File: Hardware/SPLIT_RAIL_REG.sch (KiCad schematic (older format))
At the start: 21 parts, among them Q1 PMOS, U1 TPS65130

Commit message: Annotated schematic
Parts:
- renumbered C2 to C1, C8 to C2, C9 to C3, C7 to C4, C6 to C5, C1 to C6, C3 to C7, C4 to C8, C5 to C9, R4 to R1, R5 to R3, R3 to R4, R1 to R5
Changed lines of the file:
@@
 LIBS:microchip_pic18mcu
 LIBS:microchip
+LIBS:microchip1
 LIBS:microcontrollers
 LIBS:motorola
@@
 LIBS:sensors
 LIBS:siliconi
+LIBS:special
 LIBS:stm8
 LIBS:stm32
@@
 $EndComp
 $Comp
-L GND-RESCUE-museV2 #PWR5
+L GND-RESCUE-museV2-RESCUE-museV2 #PWR01
 U 1 1 57DAC9F2
 P 5450 5000
-F 0 "#PWR5" H 5450 4750 50  0001 C CNN
+F 0 "#PWR01" H 5450 4750 50  0001 C CNN
 F 1 "GND" H 5450 4850 50  0000 C CNN
 F 2 "" H 5450 5000 50  0000 C CNN
@@
 $EndComp
 $Comp
-L C-RESCUE-museV2 C4
+L C-RESCUE-museV2 C8
 U 1 1 57DACA1F
 P 6100 4750
-F 0 "C4" H 6125 4850 50  0000 L CNN
+F 0 "C8" H 6125 4850 50  0000 L CNN
 F 1 "10nF" H 6125 4650 50  0000 L CNN
 F 2 "" H 6138 4600 50  0000 C CNN
@@
 $EndComp
 $Comp
-L C-RESCUE-museV2 C5
+L C-RESCUE-museV2 C9
 U 1 1 57DACA4A
 P 6350 4750
-F 0 "C5" H 6375 4850 50  0000 L CNN
+F 0 "C9" H 6375 4850 50  0000 L CNN
 F 1 "4.7nF" H 6375 4650 50  0000 L CNN
 F 2 "" H 6388 4600 50  0000 C CNN
@@
 $EndComp
 $Comp
-L GND-RESCUE-museV2 #PWR6
+L GND-RESCUE-museV2-RESCUE-museV2 #PWR02
 U 1 1 57DACA83
 P 6100 5000
-F 0 "#PWR6" H 6100 4750 50  0001 C CNN
+F 0 "#PWR02" H 6100 4750 50  0001 C CNN
 F 1 "GND" H 6100 4850 50  0000 C CNN
 F 2 "" H 6100 5000 50  0000 C CNN
@@
 $EndComp
 $Comp
-L GND-RESCUE-museV2 #PWR7
+L GND-RESCUE-museV2-RESCUE-museV2 #PWR03
 U 1 1 57DACA97
 P 6350 5000
-F 0 "#PWR7" H 6350 4750 50  0001 C CNN
+F 0 "#PWR03" H 6350 4750 50  0001 C CNN
 F 1 "GND" H 6350 4850 50  0000 C CNN
 F 2 "" H 6350 5000 50  0000 C CNN
@@
 $EndComp
 $Comp
-L GND-RESCUE-museV2 #PWR8
+L GND-RESCUE-museV2-RESCUE-museV2 #PWR04
 U 1 1 57DACC08
 P 6600 5000
-F 0 "#PWR8" H 6600 4750 50  0001 C CNN
+F 0 "#PWR04" H 6600 4750 50  0001 C CNN
 F 1 "GND" H 6600 4850 50  0000 C CNN
 F 2 "" H 6600 5000 50  0000 C CNN
@@
 $EndComp
 $Comp
-L GND-RESCUE-museV2 #PWR12
+L GND-RESCUE-museV2-RESCUE-museV2 #PWR05
 U 1 1 57DACD4E
 P 7550 5000
-F 0 "#PWR12" H 7550 4750 50  0001 C CNN
+F 0 "#PWR05" H 7550 4750 50  0001 C CNN
 F 1 "GND" H 7550 4850 50  0000 C CNN
 F 2 "" H 7550 5000 50  0000 C CNN
@@
 Connection ~ 6100 4200
 $Comp
-L R-RESCUE-museV2 R3
+L R-RESCUE-museV2 R4
 U 1 1 57DACF39
 P 6300 3800
-F 0 "R3" V 6200 3800 50  0000 C CNN
+F 0 "R4" V 6200 3800 50  0000 C CNN
 F 1 "1.3M" V 6300 3800 50  0000 C CNN
 F 2 "" V 6230 3800 50  0000 C CNN
@@
 $EndComp
 $Comp
-L C-RESCUE-museV2 C6
+L C-RESCUE-museV2 C5
 U 1 1 57DACF8B
 P 6500 3800
-F 0 "C6" H 6525 3900 50  0000 L CNN
+F 0 "C5" H 6525 3900 50  0000 L CNN
 F 1 "7.5pF" H 6525 3700 50  0000 L CNN
 F 2 "" H 6538 3650 50  0000 C CNN
@@
 	6300 3200 6300 3250
 $Comp
-L C-RESCUE-museV2 C7
+L C-RESCUE-museV2 C4
 U 1 1 57DADA01
 P 6850 3400
-F 0 "C7" H 6875 3500 50  0000 L CNN
+F 0 "C4" H 6875 3500 50  0000 L CNN
 F 1 "220nF" H 6875 3300 50  0000 L CNN
 F 2 "" H 6888 3250 50  0000 C CNN
@@
 Connection ~ 6300 3200
 $Comp
-L GND-RESCUE-museV2 #PWR9
+L GND-RESCUE-museV2-RESCUE-museV2 #PWR06
 U 1 1 57DADA89
 P 6850 3750
-F 0 "#PWR9" H 6850 3500 50  0001 C CNN
+F 0 "#PWR06" H 6850 3500 50  0001 C CNN
 F 1 "GND" H 6850 3600 50  0000 C CNN
 F 2 "" H 6850 3750 50  0000 C CNN
@@
 Connection ~ 4800 4200
 $Comp
-L C-RESCUE-museV2 C3
+L C-RESCUE-museV2 C7
 U 1 1 57DAE032
 P 4550 4750
-F 0 "C3" H 4575 4850 50  0000 L CNN
+F 0 "C7" H 4575 4850 50  0000 L CNN
 F 1 "100nF" H 4575 4650 50  0000 L CNN
 F 2 "" H 4588 4600 50  0000 C CNN
@@
 Connection ~ 4800 4500
 $Comp
-L R-RESCUE-museV2 R1
+L R-RESCUE-museV2 R5
 U 1 1 57DAE140
 P 4300 4500
-F 0 "R1" V 4380 4500 50  0000 C CNN
+F 0 "R5" V 4380 4500 50  0000 C CNN
 F 1 "100" V 4300 4500 50  0000 C CNN
 F 2 "" V 4230 4500 50  0000 C CNN
@@
 	4050 4500 4150 4500
 $Comp
-L GND-RESCUE-museV2 #PWR4
+L GND-RESCUE-museV2-RESCUE-museV2 #PWR07
 U 1 1 57DAE30A
 P 4550 5000
-F 0 "#PWR4" H 4550 4750 50  0001 C CNN
+F 0 "#PWR07" H 4550 4750 50  0001 C CNN
 F 1 "GND" H 4550 4850 50  0000 C CNN
 F 2 "" H 4550 5000 50  0000 C CNN
@@
 	4550 5000 4550 4900
 $Comp
-L GND-RESCUE-museV2 #PWR2
+L GND-RESCUE-museV2-RESCUE-museV2 #PWR08
 U 1 1 57DAE3B0
 P 4050 5000
-F 0 "#PWR2" H 4050 4750 50  0001 C CNN
+F 0 "#PWR08" H 4050 4750 50  0001 C CNN
 F 1 "GND" H 4050 4850 50  0000 C CNN
 F 2 "" H 4050 5000 50  0000 C CNN
@@
 Connection ~ 4550 2550
 $Comp
-L C-RESCUE-museV2 C2
+L C-RESCUE-museV2 C1
 U 1 1 57DAEAFC
 P 4550 2850
-F 0 "C2" H 4575 2950 50  0000 L CNN
+F 0 "C1" H 4575 2950 50  0000 L CNN
 F 1 "4.7uF" H 4575 2750 50  0000 L CNN
 F 2 "" H 4588 2700 50  0000 C CNN
@@
 $EndComp
 $Comp
-L GND-RESCUE-museV2 #PWR3
+L GND-RESCUE-museV2-RESCUE-museV2 #PWR09
 U 1 1 57DAEBCD
 P 4550 3050
-F 0 "#PWR3" H 4550 2800 50  0001 C CNN
+F 0 "#PWR09" H 4550 2800 50  0001 C CNN
 F 1 "GND" H 4550 2900 50  0000 C CNN
 F 2 "" H 4550 3050 50  0000 C CNN
@@
 Connection ~ 6100 2550
 $Comp
-L R-RESCUE-museV2 R5
+L R-RESCUE-museV2 R3
 U 1 1 57DAF2BE
 P 7250 3400
-F 0 "R5" V 7330 3400 50  0000 C CNN
+F 0 "R3" V 7330 3400 50  0000 C CNN
 F 1 "85.8k" V 7150 3400 50  0000 C CNN
 F 2 "" V 7180 3400 50  0000 C CNN
@@
 $EndComp
 $Comp
-L GND-RESCUE-museV2 #PWR10
+L GND-RESCUE-museV2-RESCUE-museV2 #PWR010
 U 1 1 57DAF32E
 P 7250 3750
-F 0 "#PWR10" H 7250 3500 50  0001 C CNN
+F 0 "#PWR010" H 7250 3500 50  0001 C CNN
 F 1 "GND" H 7250 3600 50  0000 C CNN
 F 2 "" H 7250 3750 50  0000 C CNN
@@
 	7250 3000 7250 3250
 $Comp
-L R-RESCUE-museV2 R4
+L R-RESCUE-museV2 R1
 U 1 1 57DAF532
 P 7050 2850
-F 0 "R4" V 7130 2850 50  0000 C CNN
+F 0 "R1" V 7130 2850 50  0000 C CNN
 F 1 "975k" V 7050 2850 50  0000 C CNN
 F 2 "" V 6980 2850 50  0000 C CNN
@@
 Connection ~ 7250 2550
 $Comp
-L C-RESCUE-museV2 C8
+L C-RESCUE-museV2 C2
 U 1 1 57DAF6D3
 P 7250 2850
-F 0 "C8" H 7275 2950 50  0000 L CNN
+F 0 "C2" H 7275 2950 50  0000 L CNN
 F 1 "6.8pF" H 7275 2750 50  0000 L CNN
 F 2 "" H 7288 2700 50  0000 C CNN
@@
 $EndComp
 $Comp
-L C-RESCUE-museV2 C9
+L C-RESCUE-museV2 C3
 U 1 1 57DAF88B
 P 7550 2850
-F 0 "C9" H 7575 2950 50  0000 L CNN
+F 0 "C3" H 7575 2950 50  0000 L CNN
 F 1 "4.7uF" H 7575 2750 50  0000 L CNN
 F 2 "" H 7588 2700 50  0000 C CNN
@@
 Connection ~ 7550 2550
 $Comp
-L GND-RESCUE-museV2 #PWR11
+L GND-RESCUE-museV2-RESCUE-museV2 #PWR011
 U 1 1 57DAF96B
 P 7550 3750
-F 0 "#PWR11" H 7550 3500 50  0001 C CNN
+F 0 "#PWR011" H 7550 3500 50  0001 C CNN
 F 1 "GND" H 7550 3600 50  0000 C CNN
 F 2 "" H 7550 3750 50  0000 C CNN
@@
 	7550 3750 7550 3000
 $Comp
-L C-RESCUE-museV2 C1
+L C-RESCUE-museV2 C6
 U 1 1 57DB07FA
 P 4050 4750
-F 0 "C1" H 4075 4850 50  0000 L CNN
+F 0 "C6" H 4075 4850 50  0000 L CNN
 F 1 "4.7uF" H 4075 4650 50  0000 L CNN
 F 2 "" H 4088 4600 50  0000 C CNN
@@
 UNSURE OF C75, C77 VALUES
 $Comp
-L +5VSB #PWR1
+L +5VSB #PWR012
 U 1 1 57F87DFC
 P 4050 2300
-F 0 "#PWR1" H 4050 2390 20  0001 C CNN
+F 0 "#PWR012" H 4050 2390 20  0001 C CNN
 F 1 "+5VSB" H 4050 2390 30  0000 C CNN
 F 2 "" H 4050 2300 60  0000 C CNN
@@
 	5550 2550 7850 2550
 $Comp
-L -15VSB #PWR14
+L -15VSB #PWR7
 U 1 1 57F88303
 P 7850 4200
-F 0 "#PWR14" H 7850 4300 50  0001 C CNN
+F 0 "#PWR7" H 7850 4300 50  0001 C CNN
 F 1 "-15VSB" H 7850 4350 50  0000 C CNN
 F 2 "" H 7850 4200 50  0000 C CNN
@@
 	7850 2550 7850 2300
 $Comp
-L +15VSB #PWR13
+L +15VSB #PWR013
 U 1 1 57F88166
 P 7850 2300
-F 0 "#PWR13" H 7850 2150 50  0001 C CNN
+F 0 "#PWR013" H 7850 2150 50  0001 C CNN
 F 1 "+15VSB" H 7850 2440 50  0000 C CNN
 F 2 "" H 7850 2300 50  0000 C CNN

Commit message: Annotation/Part Selection BOM Update
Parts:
- C2: value 6.8pF -> 6.97pF
- C5: value 7.5pF -> 5.77pF
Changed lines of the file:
@@
 LIBS:microchip_pic18mcu
 LIBS:microchip
+LIBS:microchip1
 LIBS:microcontrollers
 LIBS:motorola
@@
 LIBS:sensors
 LIBS:siliconi
+LIBS:special
 LIBS:stm8
 LIBS:stm32
@@
 $EndComp
 $Comp
-L GND-RESCUE-museV2-RESCUE-museV2 #PWR5
+L GND-RESCUE-museV2-RESCUE-museV2 #PWR01
 U 1 1 57DAC9F2
 P 5450 5000
-F 0 "#PWR5" H 5450 4750 50  0001 C CNN
+F 0 "#PWR01" H 5450 4750 50  0001 C CNN
 F 1 "GND" H 5450 4850 50  0000 C CNN
 F 2 "" H 5450 5000 50  0000 C CNN
@@
 $EndComp
 $Comp
-L GND-RESCUE-museV2-RESCUE-museV2 #PWR6
+L GND-RESCUE-museV2-RESCUE-museV2 #PWR02
 U 1 1 57DACA83
 P 6100 5000
-F 0 "#PWR6" H 6100 4750 50  0001 C CNN
+F 0 "#PWR02" H 6100 4750 50  0001 C CNN
 F 1 "GND" H 6100 4850 50  0000 C CNN
 F 2 "" H 6100 5000 50  0000 C CNN
@@
 $EndComp
 $Comp
-L GND-RESCUE-museV2-RESCUE-museV2 #PWR7
+L GND-RESCUE-museV2-RESCUE-museV2 #PWR03
 U 1 1 57DACA97
 P 6350 5000
-F 0 "#PWR7" H 6350 4750 50  0001 C CNN
+F 0 "#PWR03" H 6350 4750 50  0001 C CNN
 F 1 "GND" H 6350 4850 50  0000 C CNN
 F 2 "" H 6350 5000 50  0000 C CNN
@@
 $EndComp
 $Comp
-L GND-RESCUE-museV2-RESCUE-museV2 #PWR8
+L GND-RESCUE-museV2-RESCUE-museV2 #PWR04
 U 1 1 57DACC08
 P 6600 5000
-F 0 "#PWR8" H 6600 4750 50  0001 C CNN
+F 0 "#PWR04" H 6600 4750 50  0001 C CNN
 F 1 "GND" H 6600 4850 50  0000 C CNN
 F 2 "" H 6600 5000 50  0000 C CNN
@@
 $EndComp
 $Comp
-L GND-RESCUE-museV2-RESCUE-museV2 #PWR12
+L GND-RESCUE-museV2-RESCUE-museV2 #PWR05
 U 1 1 57DACD4E
 P 7550 5000
-F 0 "#PWR12" H 7550 4750 50  0001 C CNN
+F 0 "#PWR05" H 7550 4750 50  0001 C CNN
 F 1 "GND" H 7550 4850 50  0000 C CNN
 F 2 "" H 7550 5000 50  0000 C CNN
@@
 P 6500 3800
 F 0 "C5" H 6525 3900 50  0000 L CNN
-F 1 "7.5pF" H 6525 3700 50  0000 L CNN
+F 1 "5.77pF" H 6525 3700 50  0000 L CNN
 F 2 "" H 6538 3650 50  0000 C CNN
 F 3 "" H 6500 3800 50  0000 C CNN
@@
 Connection ~ 6300 3200
 $Comp
-L GND-RESCUE-museV2-RESCUE-museV2 #PWR9
+L GND-RESCUE-museV2-RESCUE-museV2 #PWR06
 U 1 1 57DADA89
 P 6850 3750
-F 0 "#PWR9" H 6850 3500 50  0001 C CNN
+F 0 "#PWR06" H 6850 3500 50  0001 C CNN
 F 1 "GND" H 6850 3600 50  0000 C CNN
 F 2 "" H 6850 3750 50  0000 C CNN
@@
 	4050 4500 4150 4500
 $Comp
-L GND-RESCUE-museV2-RESCUE-museV2 #PWR4
+L GND-RESCUE-museV2-RESCUE-museV2 #PWR07
 U 1 1 57DAE30A
 P 4550 5000
-F 0 "#PWR4" H 4550 4750 50  0001 C CNN
+F 0 "#PWR07" H 4550 4750 50  0001 C CNN
 F 1 "GND" H 4550 4850 50  0000 C CNN
 F 2 "" H 4550 5000 50  0000 C CNN
@@
 	4550 5000 4550 4900
 $Comp
-L GND-RESCUE-museV2-RESCUE-museV2 #PWR2
+L GND-RESCUE-museV2-RESCUE-museV2 #PWR08
 U 1 1 57DAE3B0
 P 4050 5000
-F 0 "#PWR2" H 4050 4750 50  0001 C CNN
+F 0 "#PWR08" H 4050 4750 50  0001 C CNN
 F 1 "GND" H 4050 4850 50  0000 C CNN
 F 2 "" H 4050 5000 50  0000 C CNN
@@
 $EndComp
 $Comp
-L GND-RESCUE-museV2-RESCUE-museV2 #PWR3
+L GND-RESCUE-museV2-RESCUE-museV2 #PWR09
 U 1 1 57DAEBCD
 P 4550 3050
-F 0 "#PWR3" H 4550 2800 50  0001 C CNN
+F 0 "#PWR09" H 4550 2800 50  0001 C CNN
 F 1 "GND" H 4550 2900 50  0000 C CNN
 F 2 "" H 4550 3050 50  0000 C CNN
@@
 $EndComp
 $Comp
-L GND-RESCUE-museV2-RESCUE-museV2 #PWR10
+L GND-RESCUE-museV2-RESCUE-museV2 #PWR010
 U 1 1 57DAF32E
 P 7250 3750
-F 0 "#PWR10" H 7250 3500 50  0001 C CNN
+F 0 "#PWR010" H 7250 3500 50  0001 C CNN
 F 1 "GND" H 7250 3600 50  0000 C CNN
 F 2 "" H 7250 3750 50  0000 C CNN
@@
 P 7250 2850
 F 0 "C2" H 7275 2950 50  0000 L CNN
-F 1 "6.8pF" H 7275 2750 50  0000 L CNN
+F 1 "6.97pF" H 7275 2750 50  0000 L CNN
 F 2 "" H 7288 2700 50  0000 C CNN
 F 3 "" H 7250 2850 50  0000 C CNN
@@
 Connection ~ 7550 2550
 $Comp
-L GND-RESCUE-museV2-RESCUE-museV2 #PWR11
+L GND-RESCUE-museV2-RESCUE-museV2 #PWR011
 U 1 1 57DAF96B
 P 7550 3750
-F 0 "#PWR11" H 7550 3500 50  0001 C CNN
+F 0 "#PWR011" H 7550 3500 50  0001 C CNN
 F 1 "GND" H 7550 3600 50  0000 C CNN
 F 2 "" H 7550 3750 50  0000 C CNN
@@
 UNSURE OF C75, C77 VALUES
 $Comp
-L +5VSB #PWR1
+L +5VSB #PWR012
 U 1 1 57F87DFC
 P 4050 2300
-F 0 "#PWR1" H 4050 2390 20  0001 C CNN
+F 0 "#PWR012" H 4050 2390 20  0001 C CNN
 F 1 "+5VSB" H 4050 2390 30  0000 C CNN
 F 2 "" H 4050 2300 60  0000 C CNN
@@
 	7850 2550 7850 2300
 $Comp
-L +15VSB #PWR13
+L +15VSB #PWR013
 U 1 1 57F88166
 P 7850 2300
-F 0 "#PWR13" H 7850 2150 50  0001 C CNN
+F 0 "#PWR013" H 7850 2150 50  0001 C CNN
 F 1 "+15VSB" H 7850 2440 50  0000 C CNN
 F 2 "" H 7850 2300 50  0000 C CNN

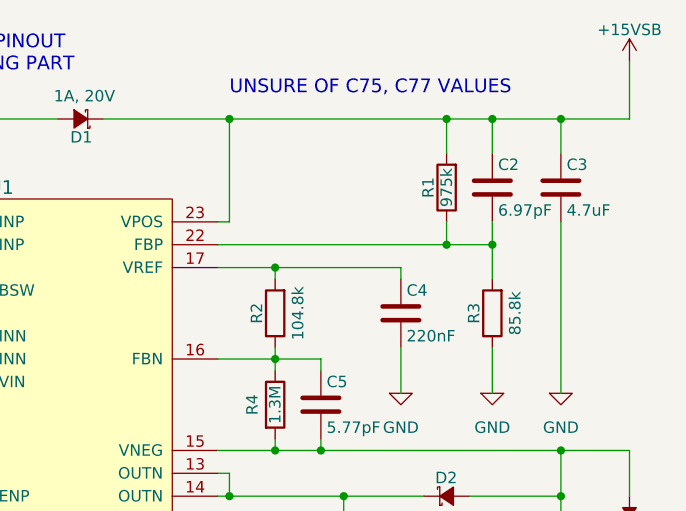
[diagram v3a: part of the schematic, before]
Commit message: Added bluetooth pair button
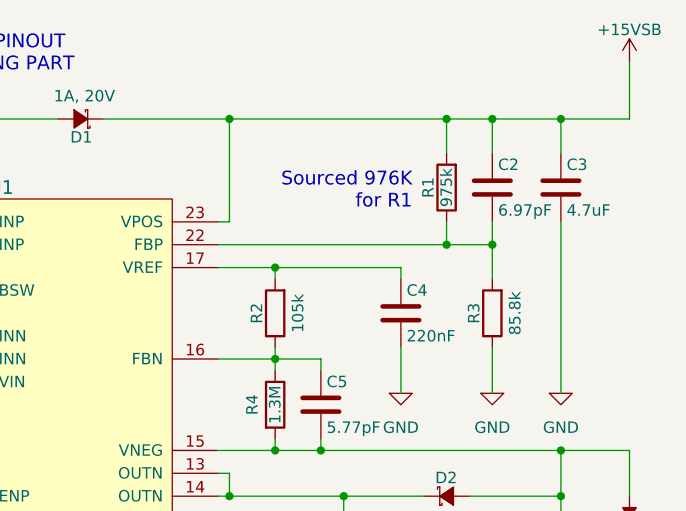
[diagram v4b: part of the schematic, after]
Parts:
- R2: value 104.8k -> 105k
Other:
- note added: "Sourced 976K\nfor R1"
- note removed: "UNSURE OF C75, C77 VALUES"
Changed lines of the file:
@@
 $EndComp
 $Comp
-L GND-RESCUE-museV2-RESCUE-museV2 #PWR01
+L GND-RESCUE-museV2-RESCUE-museV2 #PWR10
 U 1 1 57DAC9F2
 P 5450 5000
-F 0 "#PWR01" H 5450 4750 50  0001 C CNN
+F 0 "#PWR10" H 5450 4750 50  0001 C CNN
 F 1 "GND" H 5450 4850 50  0000 C CNN
 F 2 "" H 5450 5000 50  0000 C CNN
@@
 $EndComp
 $Comp
-L GND-RESCUE-museV2-RESCUE-museV2 #PWR02
+L GND-RESCUE-museV2-RESCUE-museV2 #PWR11
 U 1 1 57DACA83
 P 6100 5000
-F 0 "#PWR02" H 6100 4750 50  0001 C CNN
+F 0 "#PWR11" H 6100 4750 50  0001 C CNN
 F 1 "GND" H 6100 4850 50  0000 C CNN
 F 2 "" H 6100 5000 50  0000 C CNN
@@
 $EndComp
 $Comp
-L GND-RESCUE-museV2-RESCUE-museV2 #PWR03
+L GND-RESCUE-museV2-RESCUE-museV2 #PWR12
 U 1 1 57DACA97
 P 6350 5000
-F 0 "#PWR03" H 6350 4750 50  0001 C CNN
+F 0 "#PWR12" H 6350 4750 50  0001 C CNN
 F 1 "GND" H 6350 4850 50  0000 C CNN
 F 2 "" H 6350 5000 50  0000 C CNN
@@
 $EndComp
 $Comp
-L GND-RESCUE-museV2-RESCUE-museV2 #PWR04
+L GND-RESCUE-museV2-RESCUE-museV2 #PWR13
 U 1 1 57DACC08
 P 6600 5000
-F 0 "#PWR04" H 6600 4750 50  0001 C CNN
+F 0 "#PWR13" H 6600 4750 50  0001 C CNN
 F 1 "GND" H 6600 4850 50  0000 C CNN
 F 2 "" H 6600 5000 50  0000 C CNN
@@
 $EndComp
 $Comp
-L GND-RESCUE-museV2-RESCUE-museV2 #PWR05
+L GND-RESCUE-museV2-RESCUE-museV2 #PWR14
 U 1 1 57DACD4E
 P 7550 5000
-F 0 "#PWR05" H 7550 4750 50  0001 C CNN
+F 0 "#PWR14" H 7550 4750 50  0001 C CNN
 F 1 "GND" H 7550 4850 50  0000 C CNN
 F 2 "" H 7550 5000 50  0000 C CNN
@@
 P 6300 3400
 F 0 "R2" V 6380 3400 50  0000 C CNN
-F 1 "104.8k" V 6200 3400 50  0000 C CNN
+F 1 "105k" V 6200 3400 50  0000 C CNN
 F 2 "" V 6230 3400 50  0000 C CNN
 F 3 "" H 6300 3400 50  0000 C CNN
@@
 Connection ~ 6300 3200
 $Comp
-L GND-RESCUE-museV2-RESCUE-museV2 #PWR06
+L GND-RESCUE-museV2-RESCUE-museV2 #PWR4
 U 1 1 57DADA89
 P 6850 3750
-F 0 "#PWR06" H 6850 3500 50  0001 C CNN
+F 0 "#PWR4" H 6850 3500 50  0001 C CNN
 F 1 "GND" H 6850 3600 50  0000 C CNN
 F 2 "" H 6850 3750 50  0000 C CNN
@@
 	4050 4500 4150 4500
 $Comp
-L GND-RESCUE-museV2-RESCUE-museV2 #PWR07
+L GND-RESCUE-museV2-RESCUE-museV2 #PWR9
 U 1 1 57DAE30A
 P 4550 5000
-F 0 "#PWR07" H 4550 4750 50  0001 C CNN
+F 0 "#PWR9" H 4550 4750 50  0001 C CNN
 F 1 "GND" H 4550 4850 50  0000 C CNN
 F 2 "" H 4550 5000 50  0000 C CNN
@@
 	4550 5000 4550 4900
 $Comp
-L GND-RESCUE-museV2-RESCUE-museV2 #PWR08
+L GND-RESCUE-museV2-RESCUE-museV2 #PWR8
 U 1 1 57DAE3B0
 P 4050 5000
-F 0 "#PWR08" H 4050 4750 50  0001 C CNN
+F 0 "#PWR8" H 4050 4750 50  0001 C CNN
 F 1 "GND" H 4050 4850 50  0000 C CNN
 F 2 "" H 4050 5000 50  0000 C CNN
@@
 $EndComp
 $Comp
-L GND-RESCUE-museV2-RESCUE-museV2 #PWR09
+L GND-RESCUE-museV2-RESCUE-museV2 #PWR3
 U 1 1 57DAEBCD
 P 4550 3050
-F 0 "#PWR09" H 4550 2800 50  0001 C CNN
+F 0 "#PWR3" H 4550 2800 50  0001 C CNN
 F 1 "GND" H 4550 2900 50  0000 C CNN
 F 2 "" H 4550 3050 50  0000 C CNN
@@
 $EndComp
 $Comp
-L GND-RESCUE-museV2-RESCUE-museV2 #PWR010
+L GND-RESCUE-museV2-RESCUE-museV2 #PWR5
 U 1 1 57DAF32E
 P 7250 3750
-F 0 "#PWR010" H 7250 3500 50  0001 C CNN
+F 0 "#PWR5" H 7250 3500 50  0001 C CNN
 F 1 "GND" H 7250 3600 50  0000 C CNN
 F 2 "" H 7250 3750 50  0000 C CNN
@@
 Connection ~ 7550 2550
 $Comp
-L GND-RESCUE-museV2-RESCUE-museV2 #PWR011
+L GND-RESCUE-museV2-RESCUE-museV2 #PWR6
 U 1 1 57DAF96B
 P 7550 3750
-F 0 "#PWR011" H 7550 3500 50  0001 C CNN
+F 0 "#PWR6" H 7550 3500 50  0001 C CNN
 F 1 "GND" H 7550 3600 50  0000 C CNN
 F 2 "" H 7550 3750 50  0000 C CNN
@@
 	1    0    0    -1
 $EndComp
-Text Notes 6100 2450 0    60   ~ 0
-UNSURE OF C75, C77 VALUES
-$Comp
-L +5VSB #PWR012
+$Comp
+L +5VSB #PWR1
 U 1 1 57F87DFC
 P 4050 2300
-F 0 "#PWR012" H 4050 2390 20  0001 C CNN
+F 0 "#PWR1" H 4050 2390 20  0001 C CNN
 F 1 "+5VSB" H 4050 2390 30  0000 C CNN
 F 2 "" H 4050 2300 60  0000 C CNN
@@
 	5550 2550 7850 2550
 $Comp
-L -15VSB #PWR14
+L -15VSB #PWR7
 U 1 1 57F88303
 P 7850 4200
-F 0 "#PWR14" H 7850 4300 50  0001 C CNN
+F 0 "#PWR7" H 7850 4300 50  0001 C CNN
 F 1 "-15VSB" H 7850 4350 50  0000 C CNN
 F 2 "" H 7850 4200 50  0000 C CNN
@@
 	7850 2550 7850 2300
 $Comp
-L +15VSB #PWR013
+L +15VSB #PWR2
 U 1 1 57F88166
 P 7850 2300
-F 0 "#PWR013" H 7850 2150 50  0001 C CNN
+F 0 "#PWR2" H 7850 2150 50  0001 C CNN
 F 1 "+15VSB" H 7850 2440 50  0000 C CNN
 F 2 "" H 7850 2300 50  0000 C CNN
@@
 	1    0    0    -1
 $EndComp
+Text Notes 6900 2950 2    60   ~ 0
+Sourced 976K\nfor R1
 $EndSCHEMATC
